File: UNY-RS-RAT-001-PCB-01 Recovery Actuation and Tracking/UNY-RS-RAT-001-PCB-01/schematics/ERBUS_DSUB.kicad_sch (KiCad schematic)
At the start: 1 part, among them J2 DSUB_26_HD

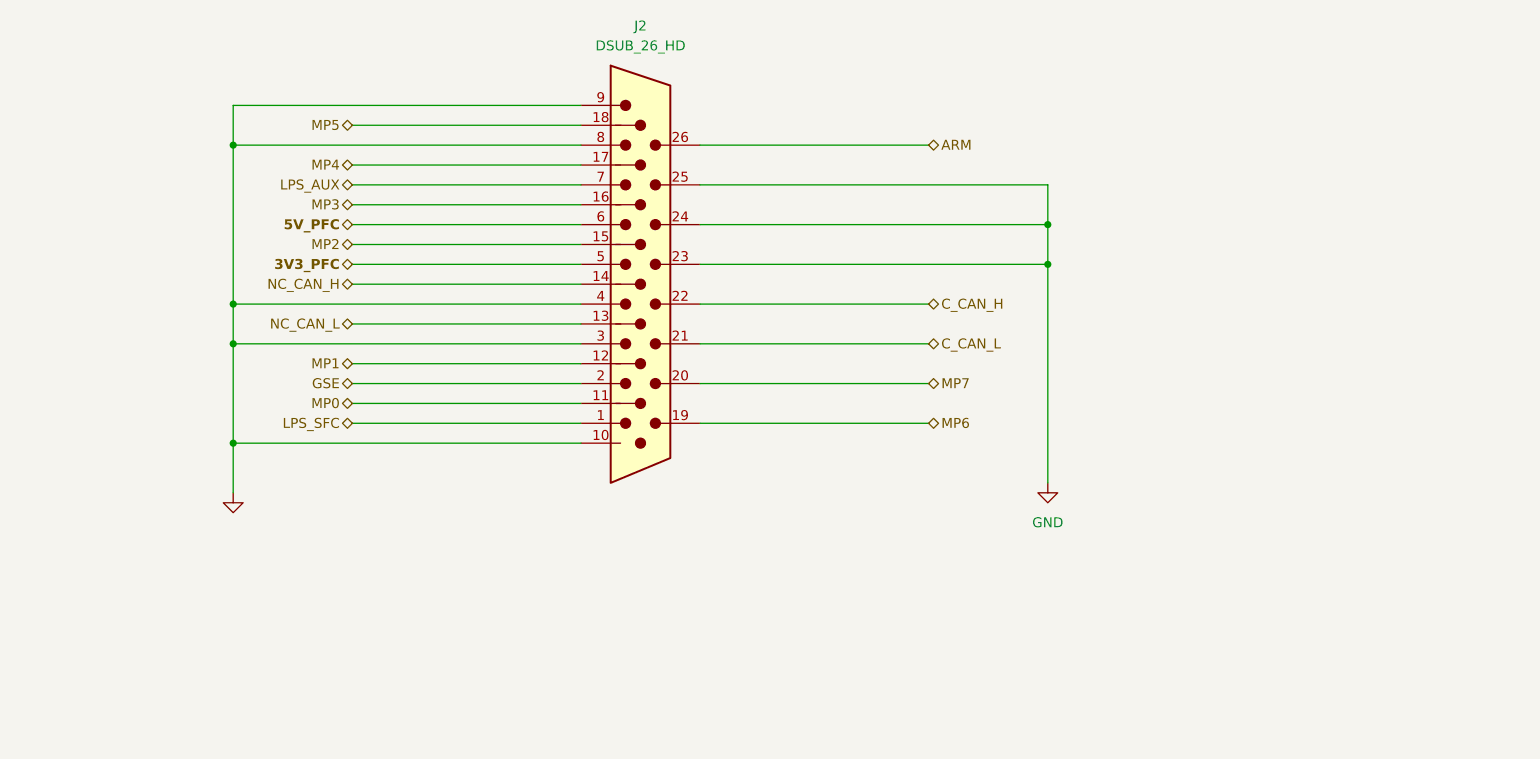
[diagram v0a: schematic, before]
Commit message: First draft for ERBUS, Power & CPU
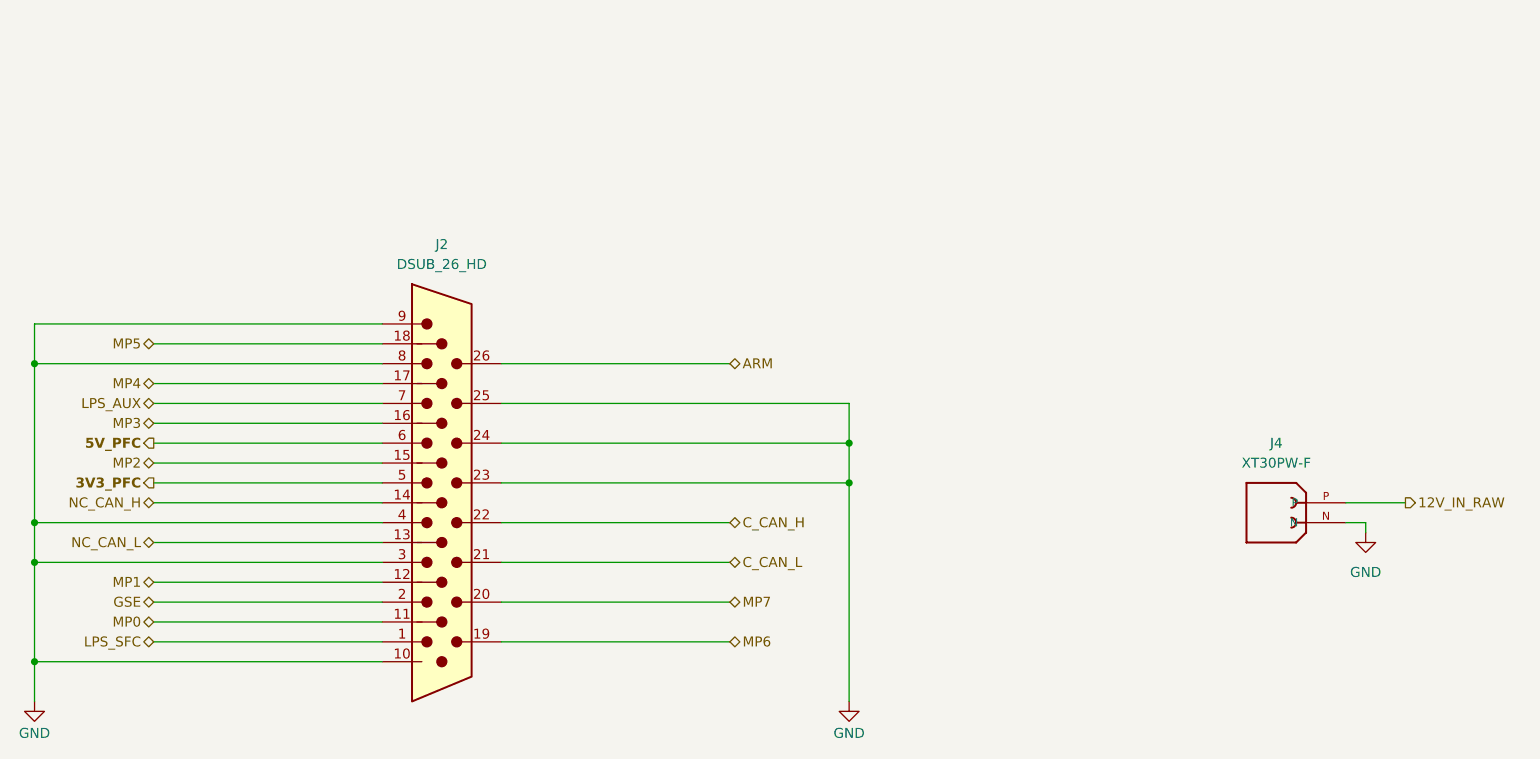
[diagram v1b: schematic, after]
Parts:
- added J4: XT30PW-F, Connector_AMASS:AMASS_XT30PW-F_1x02_P2.50mm_Horizontal, symbol XT30PW-F:XT30PW-F
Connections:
- net GND: now also J4.N
- new net 12V_IN_RAW: J4.P
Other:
- title: RAT High level schematics -> Sensor MCU
- moved on the sheet: J2

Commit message: Semi complete, missing footprints and connectors
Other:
- company: (none) -> E.R.I.G. e.V
- title: Sensor MCU -> ERBUS & Power Input
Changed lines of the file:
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@@
 	(paper "A4")
 	(title_block
-		(title "Sensor MCU")
+		(title "ERBUS & Power Input")
 		(date "2025-08-23")
 		(rev "0")
+		(company "E.R.I.G. e.V")
 	)
 	(junction
